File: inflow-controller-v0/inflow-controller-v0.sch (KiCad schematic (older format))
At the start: 16 parts, among them CN401 Conn_02x04_Odd_Even, J101 Conn_01x02, J201 Conn_01x02, J301 Conn_01x06, J401 Conn_01x02, J402 Conn_01x02, J403 Conn_01x06, SW101 SW_Push, SW201 SW_Push, SW301 SW_Push

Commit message: First pass schematic ready, board a ratsnest still
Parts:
- CN401: footprint (none) -> Connector_PinHeader_2.54mm:PinHeader_2x04_P2.54mm_Horizontal
- H301, H302, H303, H304: footprint (none) -> TestPoint:TestPoint_Loop_D2.54mm_Drill1.5mm_Beaded
- J101, J201, J401, J402: footprint (none) -> Connector_PinHeader_1.27mm:PinHeader_1x02_P1.27mm_Vertical
- J301, J403: footprint (none) -> Connector_PinHeader_1.27mm:PinHeader_1x06_P1.27mm_Vertical
- RV301, RV302: footprint (none) -> Connector_PinHeader_2.54mm:PinHeader_1x03_P2.54mm_Vertical
- SW101, SW201: footprint (none) -> Button_Switch_SMD:SW_SPST_B3S-1000
- SW301: footprint (none) -> Button_Switch_THT:SW_PUSH_6mm
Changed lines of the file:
@@
 F 0 "RV301" H 1680 2750 50  0000 R CNN
 F 1 "R_POT" H 1681 2705 50  0001 R CNN
-F 2 "" H 1750 2750 50  0001 C CNN
+F 2 "Connector_PinHeader_2.54mm:PinHeader_1x03_P2.54mm_Vertical" H 1750 2750 50  0001 C CNN
 F 3 "~" H 1750 2750 50  0001 C CNN
 	1    1750 2750
@@
 F 0 "RV302" H 2280 2750 50  0000 R CNN
 F 1 "R_POT" H 2281 2705 50  0001 R CNN
-F 2 "" H 2350 2750 50  0001 C CNN
+F 2 "Connector_PinHeader_2.54mm:PinHeader_1x03_P2.54mm_Vertical" H 2350 2750 50  0001 C CNN
 F 3 "~" H 2350 2750 50  0001 C CNN
 	1    2350 2750
-	1    0    0    -1
-$EndComp
-$Comp
-L Switch:SW_Push SW201
-U 1 1 5F4305DF
-P 1500 1850
-F 0 "SW201" H 1500 2050 50  0000 C CNN
-F 1 "SW_Push" H 1500 2044 50  0001 C CNN
-F 2 "" H 1500 2050 50  0001 C CNN
-F 3 "~" H 1500 2050 50  0001 C CNN
-	1    1500 1850
 	1    0    0    -1
 $EndComp
@@
 F 0 "SW101" H 1500 1200 50  0000 C CNN
 F 1 "SW_Push" H 1500 1194 50  0001 C CNN
-F 2 "" H 1500 1200 50  0001 C CNN
+F 2 "Button_Switch_SMD:SW_SPST_B3S-1000" H 1500 1200 50  0001 C CNN
 F 3 "~" H 1500 1200 50  0001 C CNN
 	1    1500 1000
@@
 F 0 "H301" V 1195 2453 50  0000 C CNN
 F 1 "MountingHole_Pad" V 1196 2453 50  0001 C CNN
-F 2 "" H 1050 2450 50  0001 C CNN
+F 2 "TestPoint:TestPoint_Loop_D2.54mm_Drill1.5mm_Beaded" H 1050 2450 50  0001 C CNN
 F 3 "~" H 1050 2450 50  0001 C CNN
 	1    1050 2450
@@
 F 0 "H302" V 1195 2803 50  0000 C CNN
 F 1 "MountingHole_Pad" V 1196 2803 50  0001 C CNN
-F 2 "" H 1050 2800 50  0001 C CNN
+F 2 "TestPoint:TestPoint_Loop_D2.54mm_Drill1.5mm_Beaded" H 1050 2800 50  0001 C CNN
 F 3 "~" H 1050 2800 50  0001 C CNN
 	1    1050 2800
@@
 F 0 "H303" V 1195 3203 50  0000 C CNN
 F 1 "MountingHole_Pad" V 1196 3203 50  0001 C CNN
-F 2 "" H 1050 3200 50  0001 C CNN
+F 2 "TestPoint:TestPoint_Loop_D2.54mm_Drill1.5mm_Beaded" H 1050 3200 50  0001 C CNN
 F 3 "~" H 1050 3200 50  0001 C CNN
 	1    1050 3200
@@
 F 0 "H304" V 1195 3553 50  0000 C CNN
 F 1 "MountingHole_Pad" V 1196 3553 50  0001 C CNN
-F 2 "" H 1050 3550 50  0001 C CNN
+F 2 "TestPoint:TestPoint_Loop_D2.54mm_Drill1.5mm_Beaded" H 1050 3550 50  0001 C CNN
 F 3 "~" H 1050 3550 50  0001 C CNN
 	1    1050 3550
@@
 F 0 "J201" H 2330 1842 50  0000 L CNN
 F 1 "Conn_01x02" H 2330 1751 50  0000 L CNN
-F 2 "" H 2250 1850 50  0001 C CNN
+F 2 "Connector_PinHeader_1.27mm:PinHeader_1x02_P1.27mm_Vertical" H 2250 1850 50  0001 C CNN
 F 3 "~" H 2250 1850 50  0001 C CNN
 	1    2250 1850
@@
 F 0 "CN401" H 1700 5025 50  0000 C CNN
 F 1 "Conn_02x04_Odd_Even" H 1700 5126 50  0001 C CNN
-F 2 "" H 1650 4800 50  0001 C CNN
+F 2 "Connector_PinHeader_2.54mm:PinHeader_2x04_P2.54mm_Horizontal" H 1650 4800 50  0001 C CNN
 F 3 "~" H 1650 4800 50  0001 C CNN
 	1    1650 4800
@@
 F 0 "J101" H 2330 946 50  0000 L CNN
 F 1 "Conn_01x02" H 2330 901 50  0001 L CNN
-F 2 "" H 2250 1000 50  0001 C CNN
+F 2 "Connector_PinHeader_1.27mm:PinHeader_1x02_P1.27mm_Vertical" H 2250 1000 50  0001 C CNN
 F 3 "~" H 2250 1000 50  0001 C CNN
 	1    2250 1000
@@
 F 0 "J401" H 3080 4096 50  0000 L CNN
 F 1 "Conn_01x02" H 3080 4051 50  0001 L CNN
-F 2 "" H 3000 4150 50  0001 C CNN
+F 2 "Connector_PinHeader_1.27mm:PinHeader_1x02_P1.27mm_Vertical" H 3000 4150 50  0001 C CNN
 F 3 "~" H 3000 4150 50  0001 C CNN
 	1    3000 4150
@@
 F 0 "J402" H 3080 4546 50  0000 L CNN
 F 1 "Conn_01x02" H 3080 4501 50  0001 L CNN
-F 2 "" H 3000 4600 50  0001 C CNN
+F 2 "Connector_PinHeader_1.27mm:PinHeader_1x02_P1.27mm_Vertical" H 3000 4600 50  0001 C CNN
 F 3 "~" H 3000 4600 50  0001 C CNN
 	1    3000 4600
@@
 F 0 "J301" H 3380 3146 50  0000 L CNN
 F 1 "Conn_01x06" H 3380 3151 50  0001 L CNN
-F 2 "" H 3300 3200 50  0001 C CNN
+F 2 "Connector_PinHeader_1.27mm:PinHeader_1x06_P1.27mm_Vertical" H 3300 3200 50  0001 C CNN
 F 3 "~" H 3300 3200 50  0001 C CNN
 	1    3300 3200
@@
 F 0 "J403" H 3080 5046 50  0000 L CNN
 F 1 "Conn_01x06" H 3080 5051 50  0001 L CNN
-F 2 "" H 3000 5100 50  0001 C CNN
+F 2 "Connector_PinHeader_1.27mm:PinHeader_1x06_P1.27mm_Vertical" H 3000 5100 50  0001 C CNN
 F 3 "~" H 3000 5100 50  0001 C CNN
 	1    3000 5100
@@
 F 0 "SW301" H 2150 3600 50  0000 C CNN
 F 1 "SW_Push" H 2150 3594 50  0001 C CNN
-F 2 "" H 2150 3600 50  0001 C CNN
+F 2 "Button_Switch_THT:SW_PUSH_6mm" H 2150 3600 50  0001 C CNN
 F 3 "~" H 2150 3600 50  0001 C CNN
 	1    2150 3400
@@
 Wire Wire Line
 	2350 2500 2700 2500
+$Comp
+L Switch:SW_Push SW201
+U 1 1 5F4305DF
+P 1500 1850
+F 0 "SW201" H 1500 2050 50  0000 C CNN
+F 1 "SW_Push" H 1500 2044 50  0001 C CNN
+F 2 "Button_Switch_SMD:SW_SPST_B3S-1000" H 1500 2050 50  0001 C CNN
+F 3 "~" H 1500 2050 50  0001 C CNN
+	1    1500 1850
+	1    0    0    -1
+$EndComp
 $EndSCHEMATC

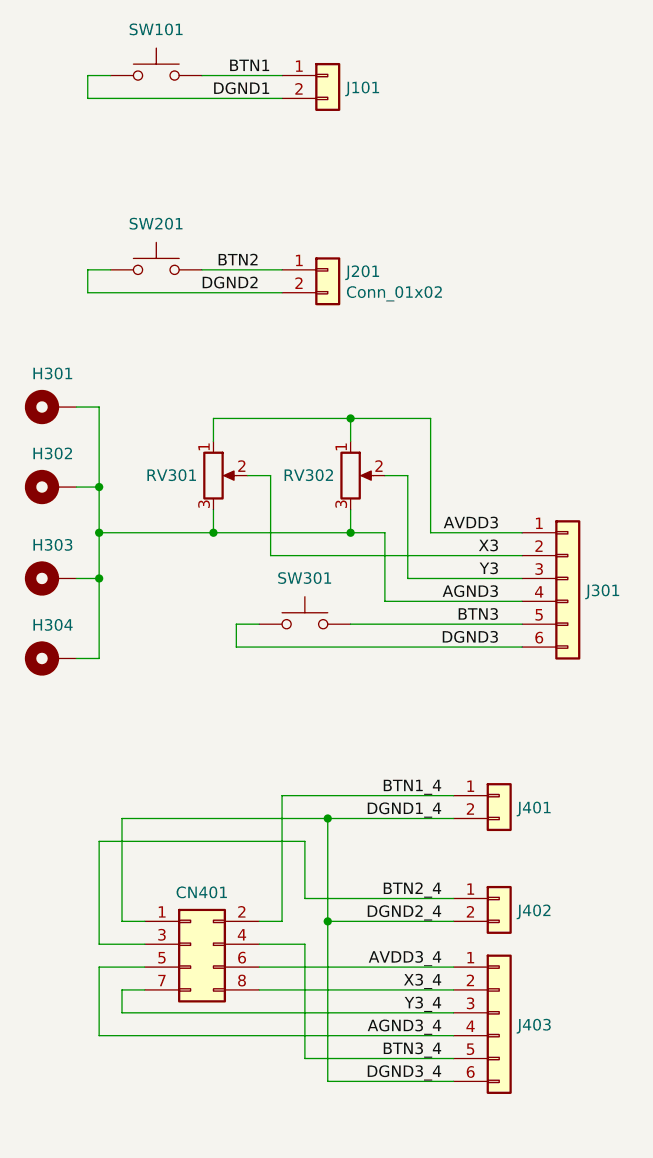
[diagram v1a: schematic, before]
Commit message: Replace joystick component on schematic with SnapEDA symbol and footprint
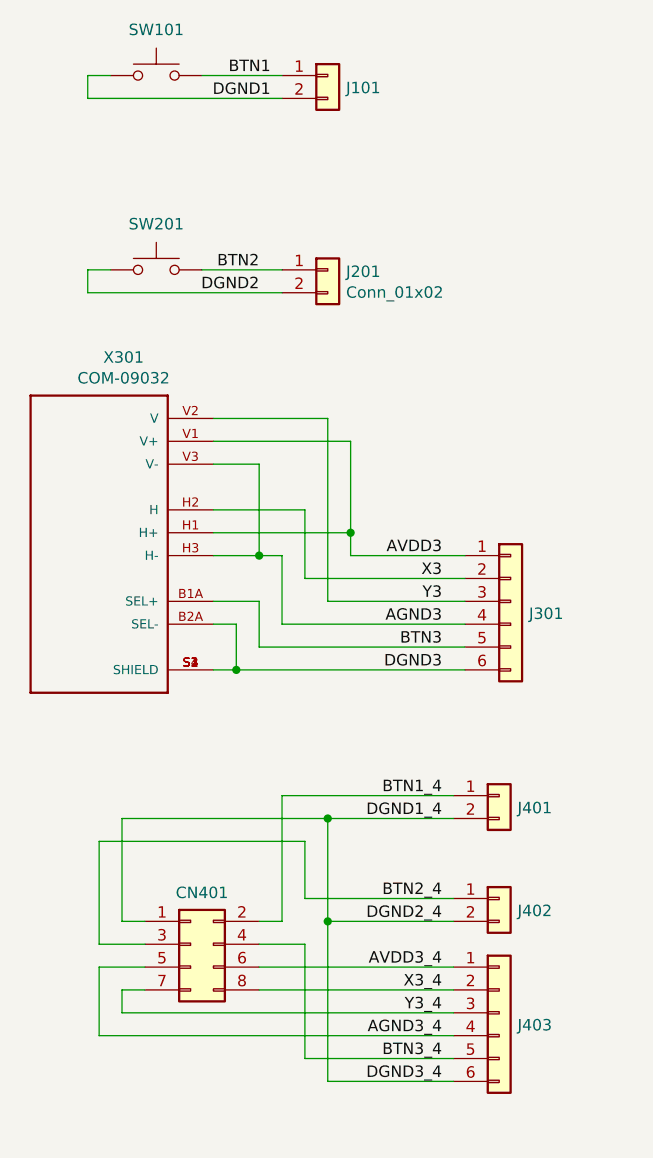
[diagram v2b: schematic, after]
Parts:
- removed H301, H302, H303, H304: MountingHole_Pad, TestPoint:TestPoint_Loop_D2.54mm_Drill1.5mm_Beaded, symbol Mechanical:MountingHole_Pad
- removed RV301, RV302: R_POT, Connector_PinHeader_2.54mm:PinHeader_1x03_P2.54mm_Vertical, symbol Device:R_POT
- removed SW301: SW_Push, Button_Switch_THT:SW_PUSH_6mm, symbol Switch:SW_Push
- added X301: COM-09032, XDCR_COM-09032, symbol COM-09032:COM-09032
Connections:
- net AGND3: now also X301.H3 (H-), X301.V3 (V-)
- net AVDD3: now also X301.H1 (H+), X301.V1 (V+)
- net BTN3: now also X301.B1A (SEL+)
- net DGND3: now also X301.B2A (SEL-), X301.S1 (SHIELD), X301.S2 (SHIELD), X301.S3 (SHIELD), X301.S4 (SHIELD)
- net X3: now also X301.H2 (H)
- net Y3: now also X301.V2 (V)
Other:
- moved on the sheet: J301
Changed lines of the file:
@@
 $EndDescr
-$Comp
-L Device:R_POT RV301
-U 1 1 5F4618CD
-P 1750 2750
-F 0 "RV301" H 1680 2750 50  0000 R CNN
-F 1 "R_POT" H 1681 2705 50  0001 R CNN
-F 2 "Connector_PinHeader_2.54mm:PinHeader_1x03_P2.54mm_Vertical" H 1750 2750 50  0001 C CNN
-F 3 "~" H 1750 2750 50  0001 C CNN
-	1    1750 2750
-	1    0    0    -1
-$EndComp
-$Comp
-L Device:R_POT RV302
-U 1 1 5F46292F
-P 2350 2750
-F 0 "RV302" H 2280 2750 50  0000 R CNN
-F 1 "R_POT" H 2281 2705 50  0001 R CNN
-F 2 "Connector_PinHeader_2.54mm:PinHeader_1x03_P2.54mm_Vertical" H 2350 2750 50  0001 C CNN
-F 3 "~" H 2350 2750 50  0001 C CNN
-	1    2350 2750
-	1    0    0    -1
-$EndComp
 $Comp
 L Switch:SW_Push SW101
@@
 $EndComp
 $Comp
-L Mechanical:MountingHole_Pad H301
-U 1 1 5F4B67C2
-P 1050 2450
-F 0 "H301" V 1195 2453 50  0000 C CNN
-F 1 "MountingHole_Pad" V 1196 2453 50  0001 C CNN
-F 2 "TestPoint:TestPoint_Loop_D2.54mm_Drill1.5mm_Beaded" H 1050 2450 50  0001 C CNN
-F 3 "~" H 1050 2450 50  0001 C CNN
-	1    1050 2450
-	0    -1   -1   0
-$EndComp
-$Comp
-L Mechanical:MountingHole_Pad H302
-U 1 1 5F4B82FD
-P 1050 2800
-F 0 "H302" V 1195 2803 50  0000 C CNN
-F 1 "MountingHole_Pad" V 1196 2803 50  0001 C CNN
-F 2 "TestPoint:TestPoint_Loop_D2.54mm_Drill1.5mm_Beaded" H 1050 2800 50  0001 C CNN
-F 3 "~" H 1050 2800 50  0001 C CNN
-	1    1050 2800
-	0    -1   -1   0
-$EndComp
-$Comp
-L Mechanical:MountingHole_Pad H303
-U 1 1 5F4B9903
-P 1050 3200
-F 0 "H303" V 1195 3203 50  0000 C CNN
-F 1 "MountingHole_Pad" V 1196 3203 50  0001 C CNN
-F 2 "TestPoint:TestPoint_Loop_D2.54mm_Drill1.5mm_Beaded" H 1050 3200 50  0001 C CNN
-F 3 "~" H 1050 3200 50  0001 C CNN
-	1    1050 3200
-	0    -1   -1   0
-$EndComp
-$Comp
-L Mechanical:MountingHole_Pad H304
-U 1 1 5F4B9909
-P 1050 3550
-F 0 "H304" V 1195 3553 50  0000 C CNN
-F 1 "MountingHole_Pad" V 1196 3553 50  0001 C CNN
-F 2 "TestPoint:TestPoint_Loop_D2.54mm_Drill1.5mm_Beaded" H 1050 3550 50  0001 C CNN
-F 3 "~" H 1050 3550 50  0001 C CNN
-	1    1050 3550
-	0    -1   -1   0
-$EndComp
-$Comp
 L Connector_Generic:Conn_01x02 J201
 U 1 1 5F4D8391
@@
 L Connector_Generic:Conn_01x06 J301
 U 1 1 5F4D4A40
-P 3300 3200
-F 0 "J301" H 3380 3146 50  0000 L CNN
-F 1 "Conn_01x06" H 3380 3151 50  0001 L CNN
-F 2 "Connector_PinHeader_1.27mm:PinHeader_1x06_P1.27mm_Vertical" H 3300 3200 50  0001 C CNN
-F 3 "~" H 3300 3200 50  0001 C CNN
-	1    3300 3200
+P 3050 3300
+F 0 "J301" H 3130 3246 50  0000 L CNN
+F 1 "Conn_01x06" H 3130 3251 50  0001 L CNN
+F 2 "Connector_PinHeader_1.27mm:PinHeader_1x06_P1.27mm_Vertical" H 3050 3300 50  0001 C CNN
+F 3 "~" H 3050 3300 50  0001 C CNN
+	1    3050 3300
 	1    0    0    -1
 $EndComp
@@
 Text Label 1950 1950 2    50   ~ 0
 DGND2
-Text Label 3000 3300 2    50   ~ 0
+Text Label 2750 3400 2    50   ~ 0
 AGND3
-Text Label 3000 3100 2    50   ~ 0
+Text Label 2750 3200 2    50   ~ 0
 X3
-Text Label 3000 3200 2    50   ~ 0
+Text Label 2750 3300 2    50   ~ 0
 Y3
-Text Label 3000 3400 2    50   ~ 0
+Text Label 2750 3500 2    50   ~ 0
 BTN3
-Text Label 3000 3500 2    50   ~ 0
+Text Label 2750 3600 2    50   ~ 0
 DGND3
 Text Label 2750 5200 2    50   ~ 0
@@
 Wire Wire Line
 	1350 5100 2800 5100
-Text Label 3000 3000 2    50   ~ 0
+Text Label 2750 3100 2    50   ~ 0
 AVDD3
-$Comp
-L Switch:SW_Push SW301
-U 1 1 5F43077F
-P 2150 3400
-F 0 "SW301" H 2150 3600 50  0000 C CNN
-F 1 "SW_Push" H 2150 3594 50  0001 C CNN
-F 2 "Button_Switch_THT:SW_PUSH_6mm" H 2150 3600 50  0001 C CNN
-F 3 "~" H 2150 3600 50  0001 C CNN
-	1    2150 3400
-	1    0    0    -1
-$EndComp
-Wire Wire Line
-	2350 2900 2350 3000
-Wire Wire Line
-	2350 3000 1750 3000
-Wire Wire Line
-	1750 3000 1750 2900
-Wire Wire Line
-	1900 2750 2000 2750
-Wire Wire Line
-	2000 2750 2000 3100
-Wire Wire Line
-	2600 3200 2600 2750
-Wire Wire Line
-	2600 2750 2500 2750
-Wire Wire Line
-	2500 3300 2500 3000
-Wire Wire Line
-	2500 3000 2350 3000
-Connection ~ 2350 3000
-Wire Wire Line
-	1750 2600 1750 2500
-Wire Wire Line
-	1750 2500 2350 2500
-Wire Wire Line
-	2700 2500 2700 3000
-Wire Wire Line
-	3100 3400 2350 3400
-Wire Wire Line
-	1950 3400 1850 3400
-Wire Wire Line
-	1850 3400 1850 3500
-Wire Wire Line
-	1850 3500 3100 3500
-Wire Wire Line
-	2500 3300 3100 3300
-Wire Wire Line
-	2600 3200 3100 3200
-Wire Wire Line
-	2700 3000 3100 3000
-Wire Wire Line
-	2000 3100 3100 3100
-Wire Wire Line
-	1150 2450 1250 2450
-Wire Wire Line
-	1250 2450 1250 2800
-Wire Wire Line
-	1250 3550 1150 3550
-Wire Wire Line
-	1150 3200 1250 3200
-Connection ~ 1250 3200
-Wire Wire Line
-	1250 3200 1250 3550
-Wire Wire Line
-	1150 2800 1250 2800
-Connection ~ 1250 2800
-Wire Wire Line
-	1250 2800 1250 3000
-Wire Wire Line
-	1250 3000 1750 3000
-Connection ~ 1250 3000
-Wire Wire Line
-	1250 3000 1250 3200
-Connection ~ 1750 3000
-Wire Wire Line
-	2350 2600 2350 2500
-Connection ~ 2350 2500
-Wire Wire Line
-	2350 2500 2700 2500
 $Comp
 L Switch:SW_Push SW201
@@
 	1    0    0    -1
 $EndComp
+$Comp
+L COM-09032:COM-09032 X301
+U 1 1 5F6866E7
+P 1250 3000
+F 0 "X301" H 1143 3767 50  0000 C CNN
+F 1 "COM-09032" H 1143 3676 50  0000 C CNN
+F 2 "XDCR_COM-09032" H 1250 3000 50  0001 L BNN
+F 3 "SparkFun Electronics" H 1250 3000 50  0001 L BNN
+F 4 "Manufacturer Recommendations" H 1250 3000 50  0001 L BNN "Field4"
+F 5 "N/A" H 1250 3000 50  0001 L BNN "Field5"
+F 6 "30.1mm" H 1250 3000 50  0001 L BNN "Field6"
+	1    1250 3000
+	-1   0    0    -1
+$EndComp
+Wire Wire Line
+	1750 3600 1850 3600
+Wire Wire Line
+	1750 3400 1850 3400
+Wire Wire Line
+	1850 3400 1850 3600
+Connection ~ 1850 3600
+Wire Wire Line
+	1850 3600 2850 3600
+Wire Wire Line
+	1750 3300 1950 3300
+Wire Wire Line
+	1950 3300 1950 3500
+Wire Wire Line
+	1950 3500 2850 3500
+Wire Wire Line
+	1750 3100 1950 3100
+Wire Wire Line
+	1750 2700 1950 2700
+Wire Wire Line
+	1950 2700 1950 3100
+Connection ~ 1950 3100
+Wire Wire Line
+	1750 3000 2350 3000
+Wire Wire Line
+	2350 3000 2350 2600
+Wire Wire Line
+	2350 2600 1750 2600
+Connection ~ 2350 3000
+Wire Wire Line
+	1750 2500 2250 2500
+Wire Wire Line
+	2250 2500 2250 3300
+Wire Wire Line
+	2250 3300 2850 3300
+Wire Wire Line
+	1750 2900 2150 2900
+Wire Wire Line
+	2150 2900 2150 3200
+Wire Wire Line
+	2150 3200 2850 3200
+Wire Wire Line
+	2850 3400 2050 3400
+Wire Wire Line
+	2050 3400 2050 3100
+Wire Wire Line
+	2050 3100 1950 3100
+Wire Wire Line
+	2350 3100 2350 3000
+Wire Wire Line
+	2350 3100 2850 3100
 $EndSCHEMATC

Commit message: Modify analog stick footprint (dimensions seemed to be wrong), route most of the PCBs
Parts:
- X301: value COM-09032 -> XB1_STICK; footprint XDCR_COM-09032 -> xb1-stick:xb1-stick; symbol COM-09032:COM-09032 -> xb1-stick:XB1_STICK
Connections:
- wire segments 59 -> 56
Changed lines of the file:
@@
 $EndComp
 $Comp
-L COM-09032:COM-09032 X301
+L xb1-stick:XB1_STICK X301
 U 1 1 5F6866E7
-P 1250 3000
-F 0 "X301" H 1143 3767 50  0000 C CNN
-F 1 "COM-09032" H 1143 3676 50  0000 C CNN
-F 2 "XDCR_COM-09032" H 1250 3000 50  0001 L BNN
-F 3 "SparkFun Electronics" H 1250 3000 50  0001 L BNN
-F 4 "Manufacturer Recommendations" H 1250 3000 50  0001 L BNN "Field4"
-F 5 "N/A" H 1250 3000 50  0001 L BNN "Field5"
-F 6 "30.1mm" H 1250 3000 50  0001 L BNN "Field6"
-	1    1250 3000
+P 1450 3200
+F 0 "X301" H 1343 3967 50  0000 C CNN
+F 1 "XB1_STICK" H 1343 3876 50  0000 C CNN
+F 2 "xb1-stick:xb1-stick" H 1450 3200 50  0001 L BNN
+F 3 "SparkFun Electronics" H 1450 3200 50  0001 L BNN
+F 4 "Manufacturer Recommendations" H 1450 3200 50  0001 L BNN "Field4"
+F 5 "N/A" H 1450 3200 50  0001 L BNN "Field5"
+F 6 "30.1mm" H 1450 3200 50  0001 L BNN "Field6"
+	1    1450 3200
 	-1   0    0    -1
 $EndComp
 Wire Wire Line
-	1750 3600 1850 3600
+	2250 3300 2850 3300
 Wire Wire Line
-	1750 3400 1850 3400
-Wire Wire Line
-	1850 3400 1850 3600
-Connection ~ 1850 3600
-Wire Wire Line
-	1850 3600 2850 3600
-Wire Wire Line
-	1750 3300 1950 3300
-Wire Wire Line
-	1950 3300 1950 3500
+	1950 3600 2850 3600
 Wire Wire Line
 	1950 3500 2850 3500
 Wire Wire Line
-	1750 3100 1950 3100
+	1950 3800 2050 3800
 Wire Wire Line
-	1750 2700 1950 2700
+	2050 3800 2050 3400
 Wire Wire Line
-	1950 2700 1950 3100
-Connection ~ 1950 3100
+	2050 2900 1950 2900
 Wire Wire Line
-	1750 3000 2350 3000
+	1950 3300 2050 3300
+Connection ~ 2050 3300
 Wire Wire Line
-	2350 3000 2350 2600
+	2050 3300 2050 2900
 Wire Wire Line
-	2350 2600 1750 2600
-Connection ~ 2350 3000
+	2050 3400 2850 3400
+Connection ~ 2050 3400
 Wire Wire Line
-	1750 2500 2250 2500
+	2050 3400 2050 3300
 Wire Wire Line
-	2250 2500 2250 3300
+	2150 3200 1950 3200
 Wire Wire Line
-	2250 3300 2850 3300
+	1950 3100 2350 3100
 Wire Wire Line
-	1750 2900 2150 2900
+	2350 3100 2350 3200
 Wire Wire Line
-	2150 2900 2150 3200
+	2350 3200 2850 3200
 Wire Wire Line
-	2150 3200 2850 3200
+	2850 3100 2450 3100
 Wire Wire Line
-	2850 3400 2050 3400
+	2450 3100 2450 2800
 Wire Wire Line
-	2050 3400 2050 3100
+	1950 2800 2150 2800
 Wire Wire Line
-	2050 3100 1950 3100
+	2150 3200 2150 2800
+Connection ~ 2150 2800
 Wire Wire Line
-	2350 3100 2350 3000
+	2150 2800 2450 2800
 Wire Wire Line
-	2350 3100 2850 3100
+	1950 2700 2250 2700
+Wire Wire Line
+	2250 2700 2250 3300
 $EndSCHEMATC

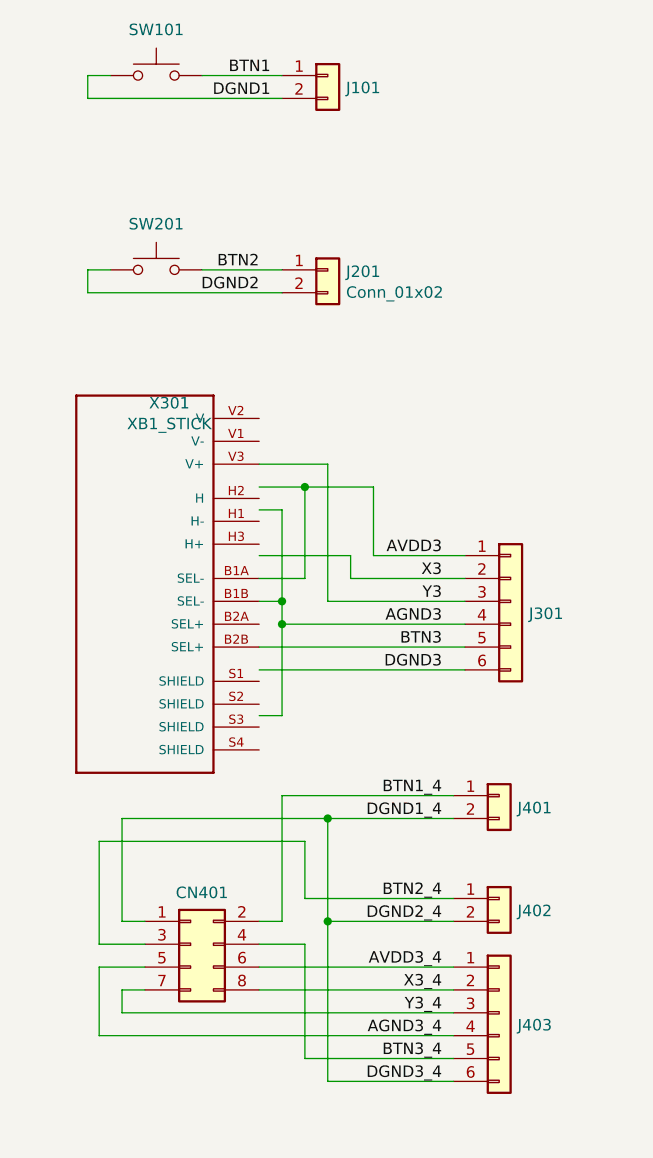
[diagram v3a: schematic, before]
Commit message: Update xb1-stick joystick footprint and symbol
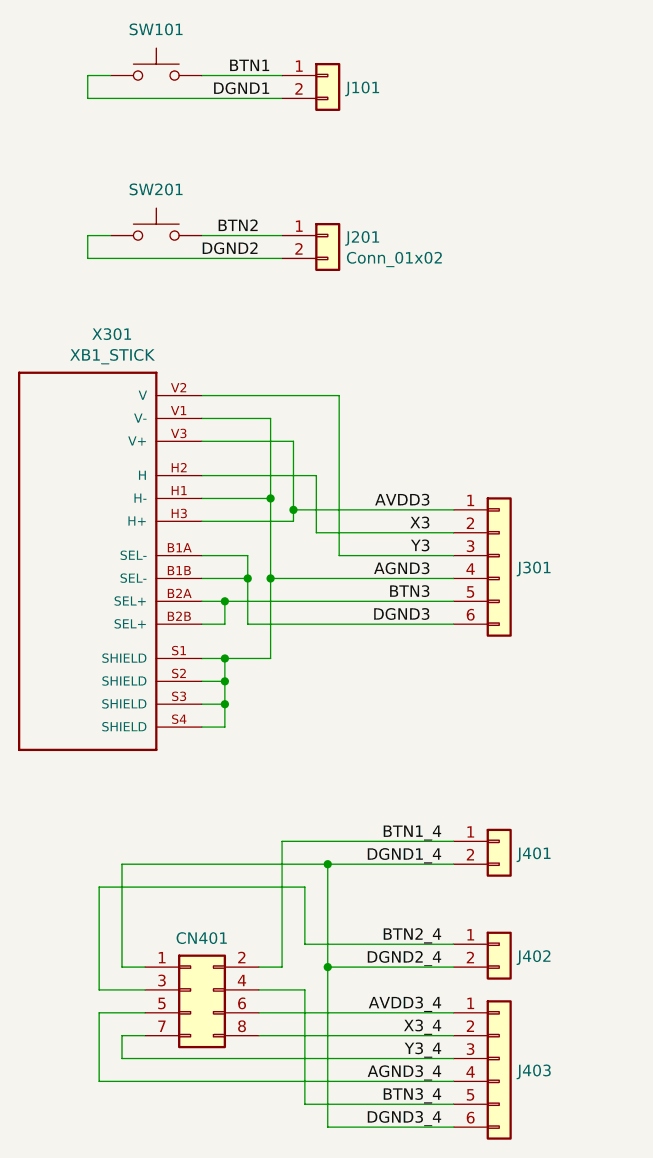
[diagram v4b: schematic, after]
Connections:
- wire segments 56 -> 69
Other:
- moved on the sheet: CN401, J201, J301, J401, J402, J403, SW201

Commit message: v0 out for production
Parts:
- renumbered J201 to J202, J301 to J303
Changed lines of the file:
@@
 $EndComp
 $Comp
-L Connector_Generic:Conn_01x02 J201
+L Connector_Generic:Conn_01x02 J202
 U 1 1 5F4D8391
 P 2250 1700
-F 0 "J201" H 2330 1692 50  0000 L CNN
+F 0 "J202" H 2330 1692 50  0000 L CNN
 F 1 "Conn_01x02" H 2330 1601 50  0000 L CNN
 F 2 "Connector_PinHeader_1.27mm:PinHeader_1x02_P1.27mm_Vertical" H 2250 1700 50  0001 C CNN
@@
 $EndComp
 $Comp
-L Connector_Generic:Conn_01x06 J301
+L Connector_Generic:Conn_01x06 J303
 U 1 1 5F4D4A40
 P 3000 3100
-F 0 "J301" H 3080 3046 50  0000 L CNN
+F 0 "J303" H 3080 3046 50  0000 L CNN
 F 1 "Conn_01x06" H 3080 3051 50  0001 L CNN
 F 2 "Connector_PinHeader_1.27mm:PinHeader_1x06_P1.27mm_Vertical" H 3000 3100 50  0001 C CNN
